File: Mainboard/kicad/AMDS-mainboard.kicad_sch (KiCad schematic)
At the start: 27 parts

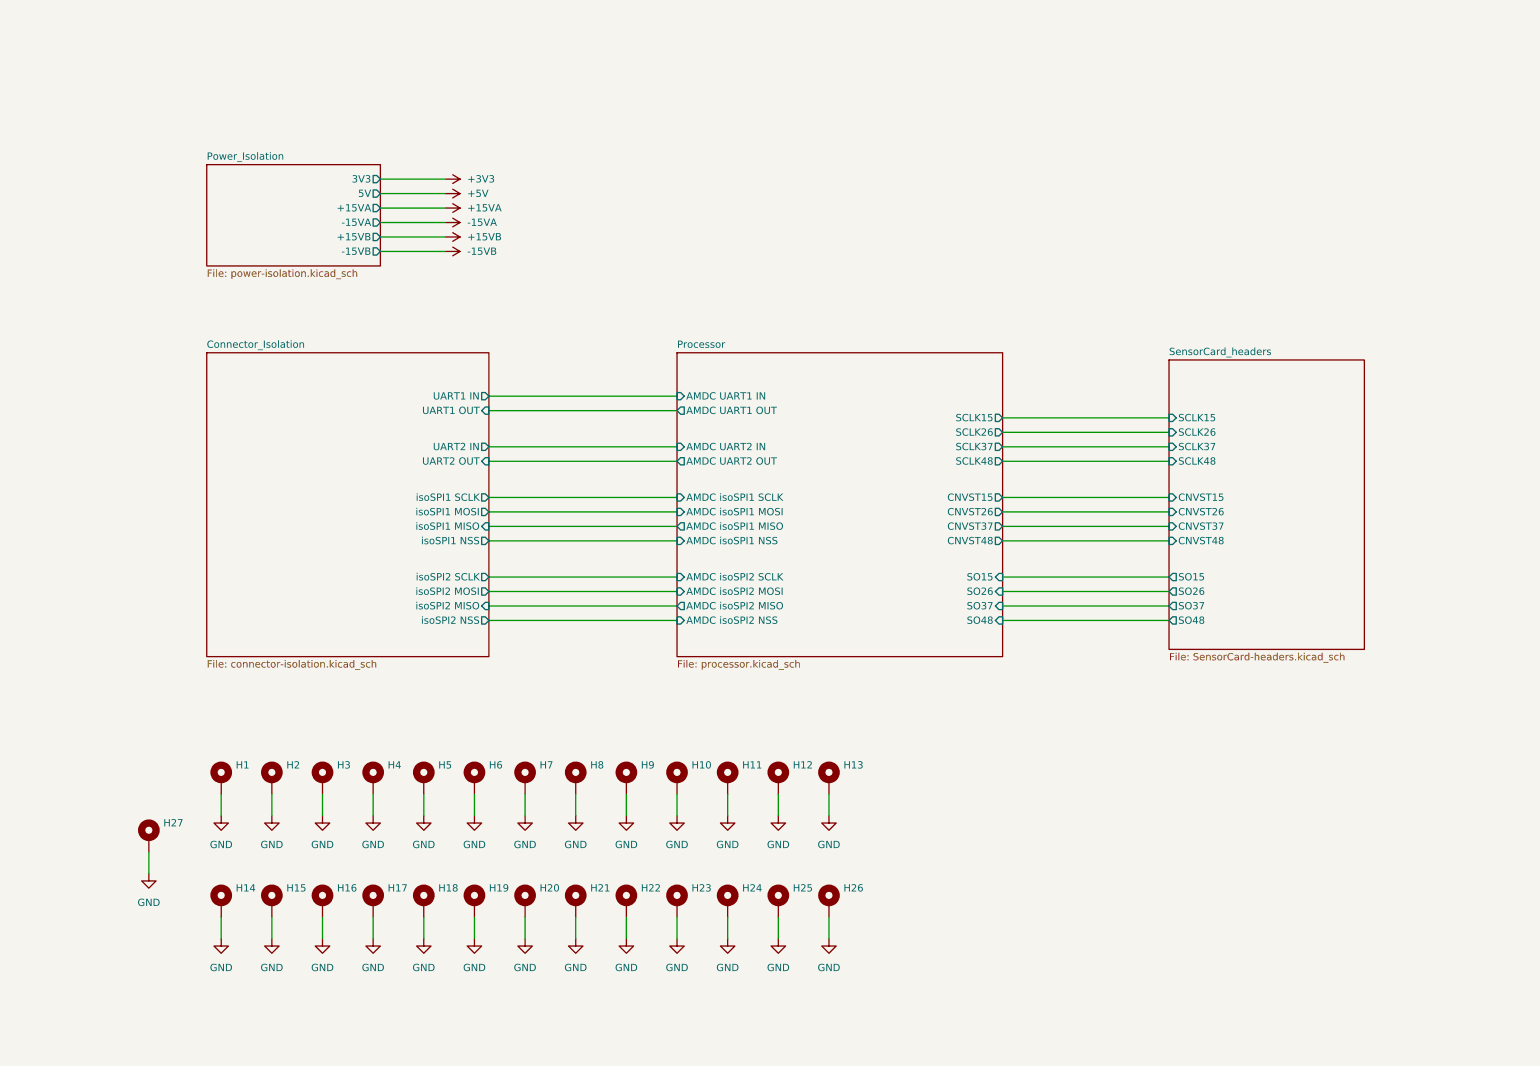
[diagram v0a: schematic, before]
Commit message: add initial mechanical components
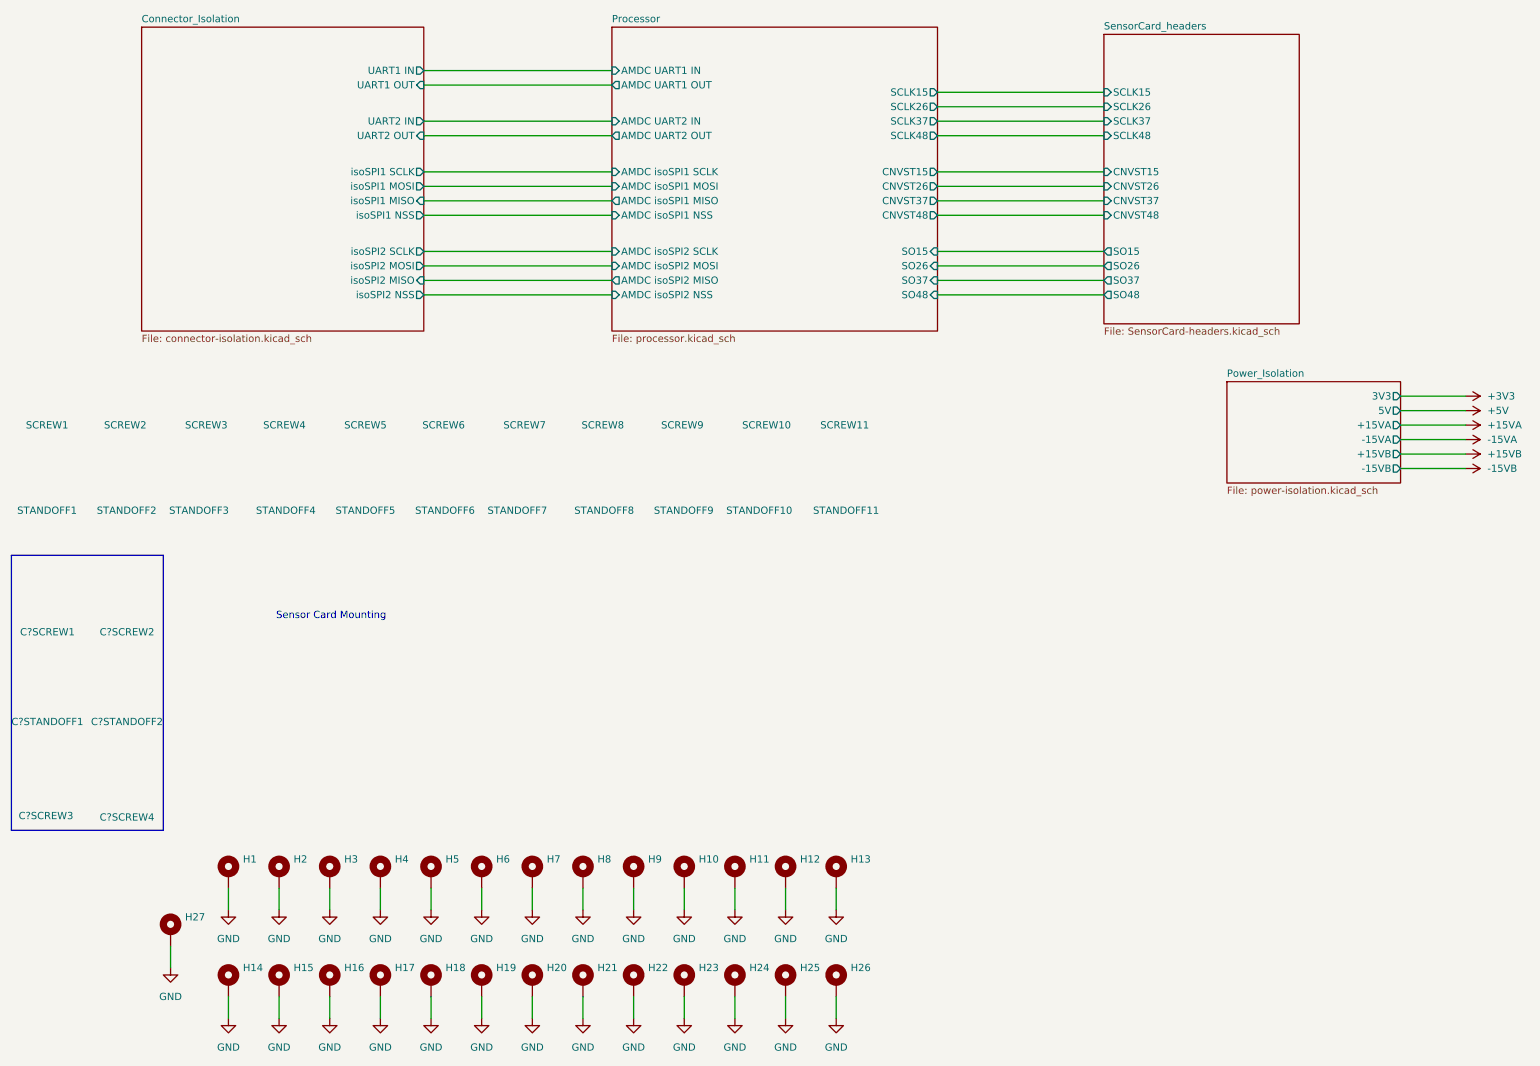
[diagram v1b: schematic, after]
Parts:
- added C?SCREW1, C?SCREW2, C?SCREW3, C?SCREW4, C?SCREW5, SCREW1, SCREW10, SCREW11, SCREW2, SCREW3, SCREW4, SCREW5, SCREW6, SCREW7, SCREW8, SCREW9: ~, symbol ST_MCU_and_Current_Sensing:KEY1046-ND
- added C?STANDOFF1, C?STANDOFF2: ~, symbol ST_MCU_and_Current_Sensing:1772-3771-ND
- added STANDOFF1, STANDOFF10, STANDOFF11, STANDOFF2, STANDOFF3, STANDOFF4, STANDOFF5, STANDOFF6, STANDOFF7, STANDOFF8, STANDOFF9: ~, symbol ST_MCU_and_Current_Sensing:36-1656-ND
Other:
- note added: "Sensor Card Mounting"
- moved on the sheet: H1, H10, H11, H12, H13, H14, H15, H16, H17, H18, H19, H2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
